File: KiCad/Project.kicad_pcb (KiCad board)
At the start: 2 copper layers, 138.4 x 74.9 mm, 73 parts, among them IC1 ATMEGA328-P, IC2 ATTINY85-P, IC3 ATTINY85-P, M1 Motor, M2 Motor, P1 CONN_02X03, P2 CONN_01X02, P3 CONN_01X02, P4 CONN_01X02, P5 CONN_02X04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

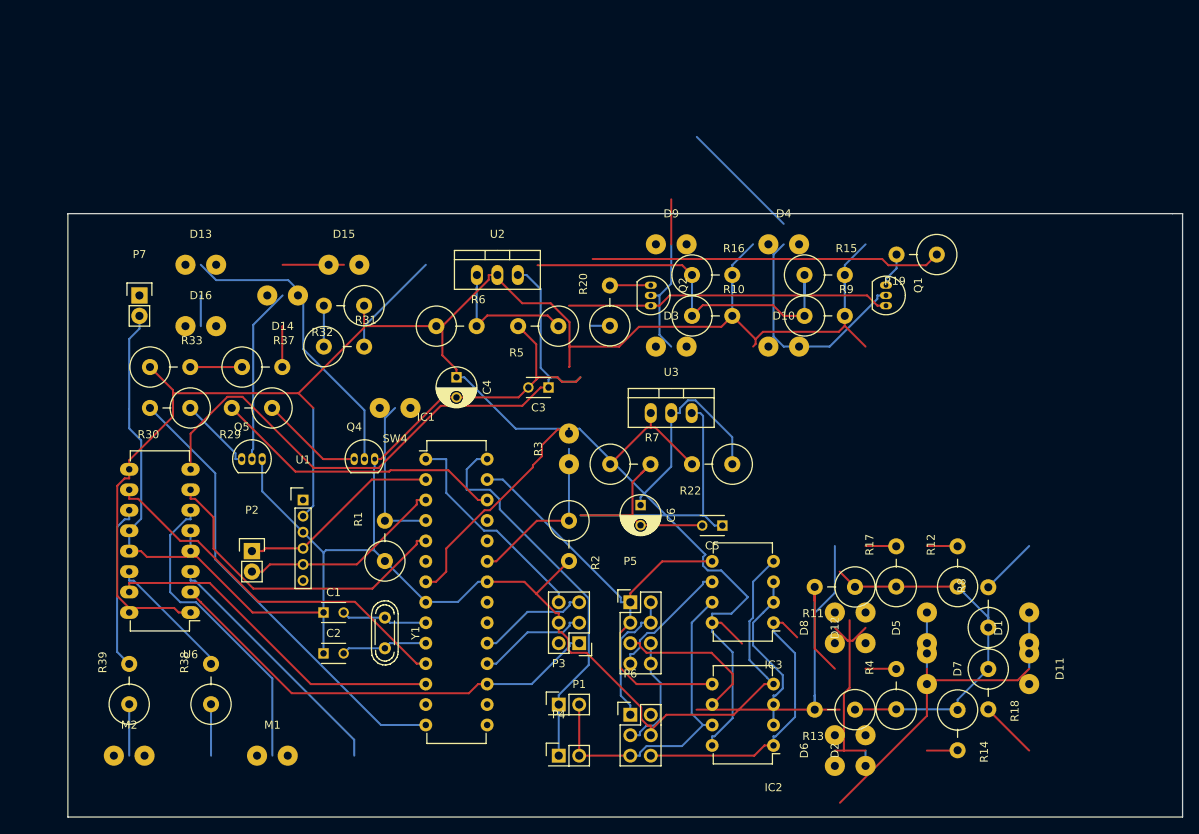
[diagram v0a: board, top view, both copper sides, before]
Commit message: Updated the pcb to smaller size and footprints
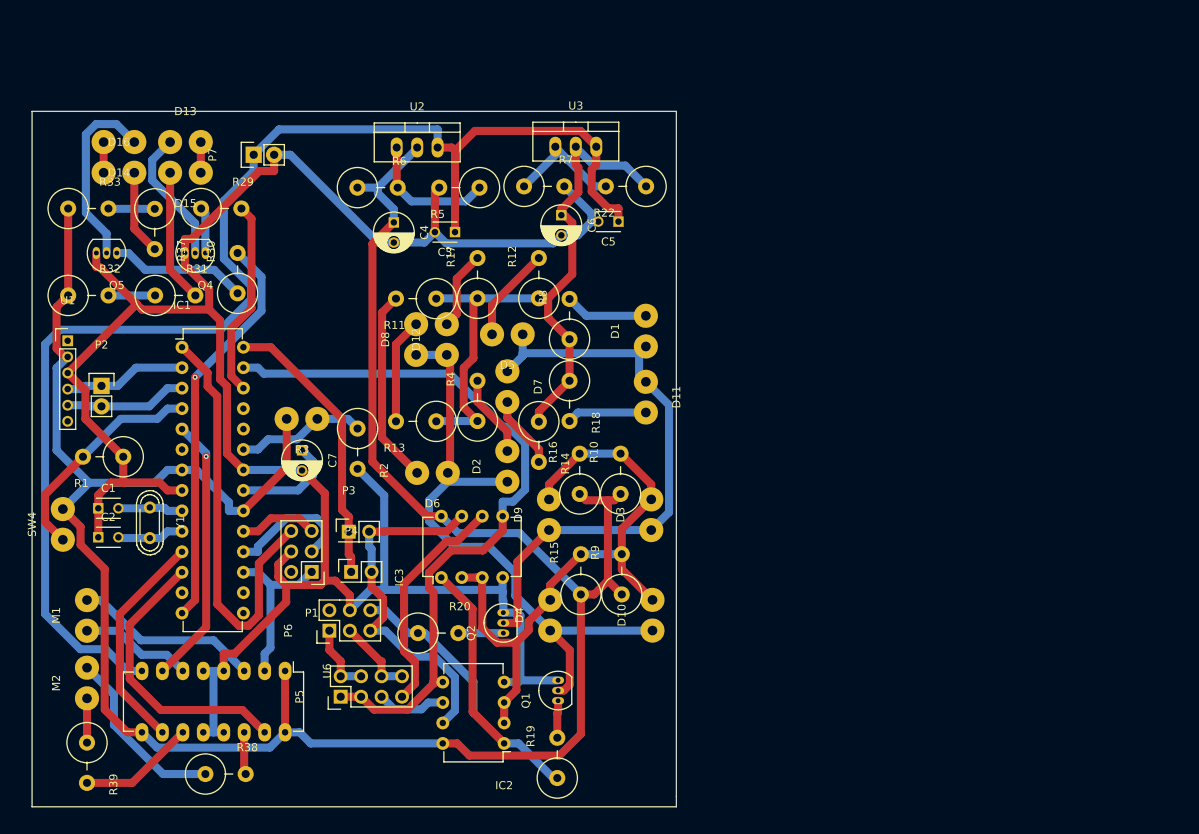
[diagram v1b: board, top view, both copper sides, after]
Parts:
- added C7: CP, Capacitors_ThroughHole:C_Radial_D5_L6_P2.5, F.Cu at (87.5, 84.0)
- D1, D10, D11, D12, D13, D14, D15, D16, D2, D3, D4, D5, D6, D7, D8, D9, M1, M2, R3, SW4: footprint Wire_Pads:SolderWirePad_2x_1mmDrill -> Holes:SolderWirePad1mmmodified
- moved R19 76.8 mm to (119.2, 122.2), turned to 90 degrees
- moved Q1 65.7 mm to (119.3, 115.1), turned to 90 degrees
- moved D5 63.6 mm to (113.0, 69.6), turned to 180 degrees
- moved R12 63.1 mm to (116.9, 62.6)
- moved R14 63.1 mm to (116.9, 82.9)
- moved R18 63.1 mm to (120.7, 77.9)
- moved R8 63.1 mm to (120.7, 67.7)
- moved R4 63.1 mm to (109.3, 77.9)
- moved D12 63.1 mm to (105.5, 70.2)
- moved D8 63.1 mm to (101.7, 70.2)
- moved R11 63.1 mm to (101.7, 65.2)
- moved R13 63.1 mm to (101.7, 80.4)
- moved R17 63.1 mm to (109.3, 62.6)
- moved D7 62.8 mm to (113.0, 76.1)
- moved D6 60.7 mm to (103.7, 86.8), turned to 180 degrees
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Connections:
- IC1 pad 13: Net-(IC1-Pad13) -> (no net)
- IC1 pad 15: Net-(IC1-Pad15) -> (no net)
- IC1 pad 16: Net-(IC1-Pad16) -> (no net)
- IC1 pad 20: Net-(IC1-Pad20) -> /IR/5V
- IC1 pad 24: Net-(IC1-Pad24) -> (no net)
- IC1 pad 25: Net-(IC1-Pad25) -> (no net)
- IC1 pad 6: Net-(IC1-Pad6) -> (no net)
- P1 pad 2: Net-(P1-Pad2) -> (no net)
- P6 pad 2: Net-(P6-Pad2) -> (no net)
- P7 pad 1: Net-(P7-Pad1) -> /Motor/9V
- U1 pad 1: Net-(U1-Pad1) -> (no net)
- U1 pad 6: Net-(U1-Pad6) -> (no net)
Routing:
- net (no net): track 84.8 -> 0.00 mm
- net /IR/5V: track 223.2 -> 295.1 mm
- net Net-(IC1-Pad23): track 88.1 -> 16.3 mm, vias 1 -> 0
- net /Motor/9V: track 111.3 -> 167.1 mm
- net Net-(D10-Pad1): track 30.6 -> 77.6 mm
- net /Motor/Forw.: track 56.3 -> 20.8 mm
- net /IR/SDA: track 58.3 -> 91.6 mm
- net Net-(IC2-Pad1): track 84.0 -> 57.9 mm
- net Net-(IC1-Pad1): track 27.0 -> 52.7 mm
- net Net-(M1-Pad1): track 38.3 -> 14.0 mm
- net Net-(D14-Pad1): track 42.9 -> 23.3 mm
- net /Motor/Left: track 46.4 -> 27.8 mm
- net /Motor/Styrning: track 6.39 -> 22.4 mm
- net Net-(C7-Pad1): track 0.00 -> 13.1 mm
- net /IR/SCL: track 48.2 -> 35.4 mm
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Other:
- board size 138.4 x 74.9 mm -> 80 x 86.4 mm
- net class Default: trace_width 0.25 -> 1

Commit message: Small updates
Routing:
- net /IR/5V: track 295.1 -> 0.00 mm
- net GND: track 293.7 -> 0.00 mm
- net /Motor/9V: track 167.1 -> 0.00 mm
- net /IR/SDA: track 91.6 -> 0.00 mm
- net /IR/3V: track 86.6 -> 0.00 mm
- net /IR/Signal: track 78.9 -> 0.00 mm
- net Net-(D10-Pad1): track 77.6 -> 0.00 mm
- net Net-(D1-Pad1): track 73.0 -> 0.00 mm
- net Net-(IC2-Pad1): track 57.9 -> 0.00 mm
- net Net-(IC1-Pad1): track 52.7 -> 0.00 mm
- net /lights/Brake: track 50.0 -> 0.00 mm, vias 1 -> 0
- net Net-(IC2-Pad7): track 45.2 -> 0.00 mm
- net /Motor/Right: track 35.4 -> 0.00 mm
- net /IR/SCL: track 35.4 -> 0.00 mm
- net /Motor/Backw.: track 33.5 -> 0.00 mm, vias 1 -> 0
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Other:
- board outline removed

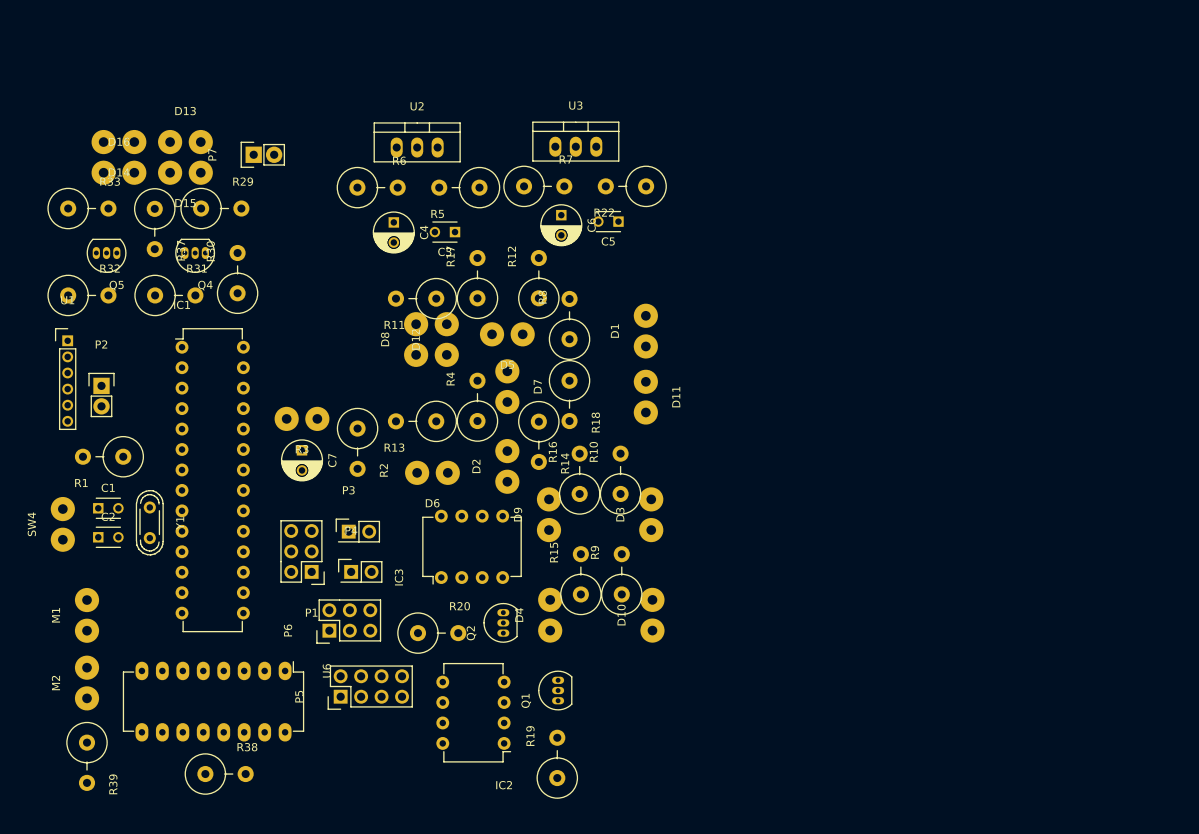
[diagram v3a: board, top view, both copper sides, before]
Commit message: Changed size of PCB and started with BT communication
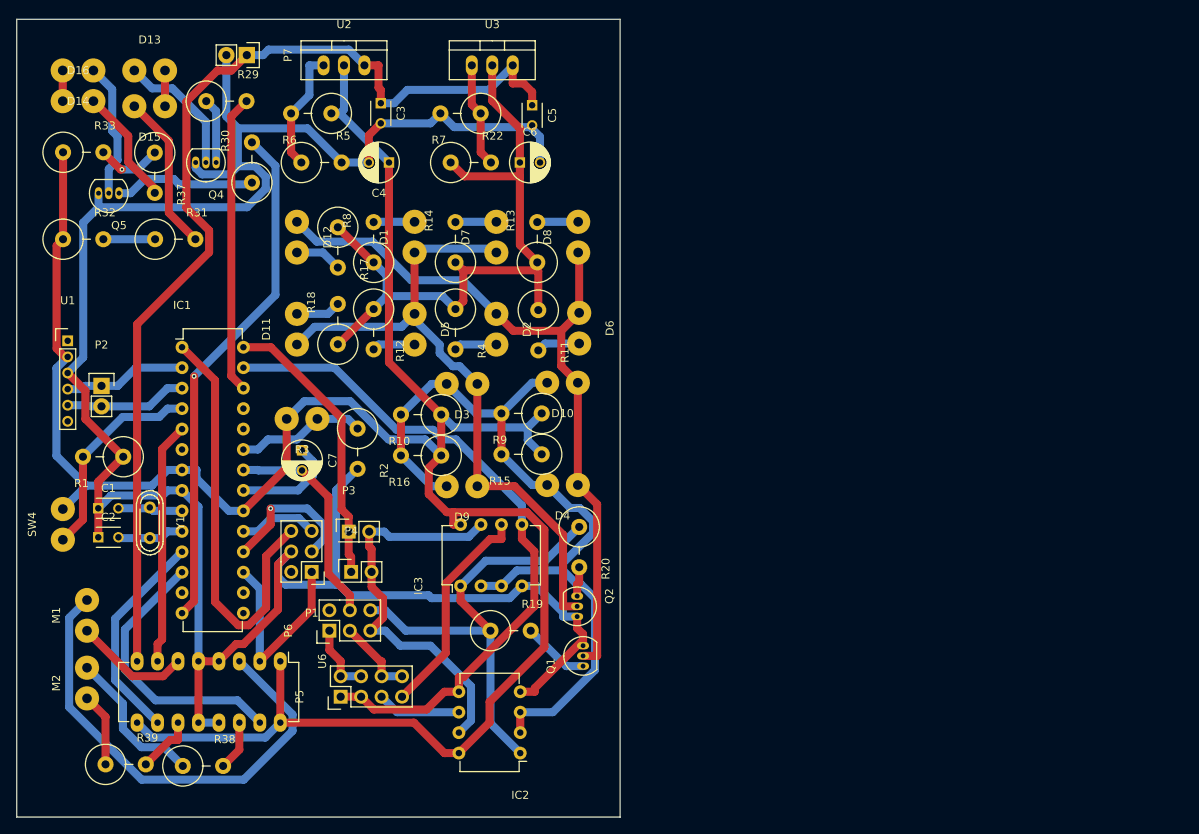
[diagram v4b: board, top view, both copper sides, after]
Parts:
- moved D11 44.1 mm to (86.9, 69.0), turned to 90 degrees
- moved D1 31.0 mm to (101.5, 57.5)
- moved D10 31.0 mm to (119.8, 75.6), turned to 180 degrees
- moved R18 30.3 mm to (91.9, 68.3), turned to 90 degrees
- moved D3 28.6 mm to (107.4, 75.8), turned to 180 degrees
- moved R14 26.9 mm to (106.6, 58.2), turned to 90 degrees
- moved R13 26.8 mm to (116.7, 58.2), turned to 90 degrees
- moved R8 26.1 mm to (96.4, 58.2)
- moved R10 25.8 mm to (102.3, 79.6), turned to 180 degrees
- moved D6 25.6 mm to (121.9, 68.8), turned to 270 degrees
- moved D8 23.8 mm to (121.8, 57.5)
- moved R9 23.5 mm to (114.8, 79.4), turned to 180 degrees
- moved D12 22.5 mm to (86.9, 57.5), turned to 270 degrees
- moved R12 21.5 mm to (96.4, 69.0), turned to 270 degrees
- moved R20 20.5 mm to (121.9, 96.0), turned to 270 degrees
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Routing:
- net GND: track 0.00 -> 312.9 mm
- net /IR/5V: track 0.00 -> 288.0 mm
- net /Motor/9V: track 0.00 -> 131.7 mm
- net /IR/Signal: track 0.00 -> 102.0 mm
- net Net-(D10-Pad1): track 0.00 -> 93.1 mm
- net /IR/3V: track 0.00 -> 86.7 mm
- net /IR/SDA: track 0.00 -> 85.9 mm
- net Net-(D1-Pad1): track 0.00 -> 83.1 mm
- net /lights/Brake: track 0.00 -> 64.5 mm, vias 0 -> 1
- net /Motor/Vroom: track 0.00 -> 59.6 mm
- net Net-(IC2-Pad1): track 0.00 -> 57.6 mm
- net Net-(IC1-Pad1): track 0.00 -> 52.6 mm
- net Net-(IC2-Pad7): track 0.00 -> 50.2 mm
- net /lights/Headlight: track 0.00 -> 37.0 mm
- net /IR/SCL: track 0.00 -> 35.4 mm
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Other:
- board outline added: 74.9 x 99.1 mm
